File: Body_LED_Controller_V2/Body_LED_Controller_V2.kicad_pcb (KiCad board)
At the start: 4 copper layers, 123 x 78 mm, 101 parts, among them J1 Body Servos, J10 USB_B_Micro, J11 USB_B_Micro, J12 UnSW_BATT_IN, J13 Batt Level LEDS, J14 DomeControllerUSB, J15 DomePlateControllerUSB, J16 UnSW_BATT_PASS, J17 RADH_POW, J18 RASP_POW, J19 5V_OUT_3, J2 Body Servos, J20 ICSP, J21 DomeElectronicsPowerIn, J22 DB25_Female_MountingHoles, J23 Amplifier_POW, J24 Future, J25 Stealth, J26 RADH, J27 VU Data Panel, J3 Conn_02x10_Odd_Even, J4 LDP, J5 Coin Slots, J6 Batt Level LEDS, J7 Data Panel/ CBI, J8 Spectrum Analyzer, J9 Maintenance, SW1 SW_Push, SW2 SW_Push, U1 ATMEGA256016AU, U14 D36V50F5-STEPDOWN, U2 CH340C, U3 CJ2301_S1, U4 ESP32-WROOM-32D_16MB_, U5 CH340C, U6 UMH3N, U7 ME6211C33M5G, U8 CJ2301_S1, Y1 16MHz

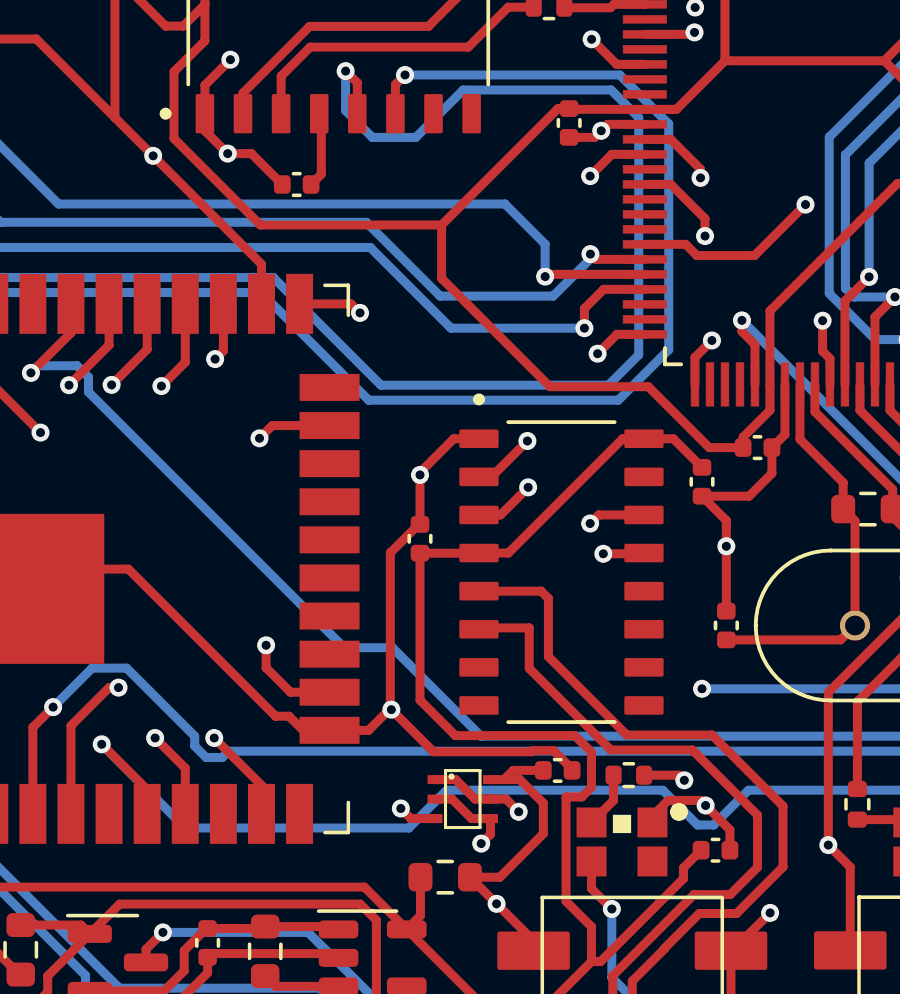
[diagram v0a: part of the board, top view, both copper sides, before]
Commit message: Added custom libraries and updated the Kill Switch (Remote)
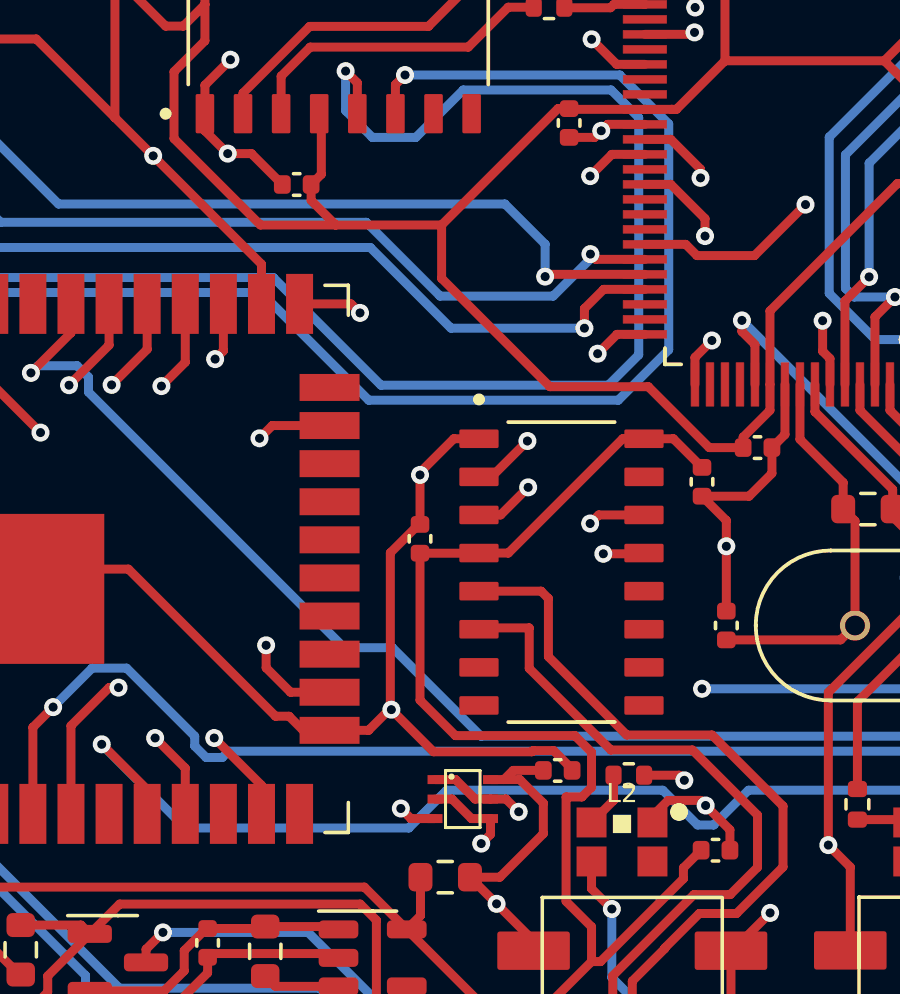
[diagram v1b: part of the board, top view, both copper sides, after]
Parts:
- J22: value DB25_Female_MountingHoles -> DB25_Male_MountingHoles
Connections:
- C5 pad 1: Net-(C5-Pad1) -> +5V_BL
- U2 pad 4: Net-(C5-Pad1) -> +5V_BL
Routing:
- net +5V_BL: track 154.4 -> 158.6 mm
- net Net-(C5-Pad1): track 2.53 -> 0.00 mm

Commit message: Working on boards
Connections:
- C5 pad 1: +5V_BL -> Net-(C5-Pad1)
- U2 pad 4: +5V_BL -> Net-(C5-Pad1)
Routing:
- net +5V_BL: track 158.6 -> 154.4 mm
- net Net-(C5-Pad1): track 0.00 -> 2.53 mm
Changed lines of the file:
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@@
   (net 190 "unconnected-(U1-Pad43)")
   (net 191 "unconnected-(U1-Pad44)")
+  (net 192 "Net-(C5-Pad1)")
   (footprint "Resistor_SMD:R_0402_1005Metric" (layer "F.Cu")
     (at 170.47 58.04 90)
@@
     (fp_line (start -0.5 0.25) (end -0.5 -0.25) (layer "F.Fab") (width 0.1))
     (pad "1" smd roundrect locked (at -0.48 0 180) (size 0.56 0.62) (layers "F.Cu" "F.Paste" "F.Mask") (roundrect_rratio 0.25)
-      (net 24 "+5V_BL") (pintype "passive"))
+      (net 192 "Net-(C5-Pad1)") (pintype "passive"))
     (pad "2" smd roundrect locked (at 0.48 0 180) (size 0.56 0.62) (layers "F.Cu" "F.Paste" "F.Mask") (roundrect_rratio 0.25)
       (net 2 "GND") (pintype "passive"))
@@
       (net 75 "Net-(R2-Pad1)") (pinfunction "RXD") (pintype "input"))
     (pad "4" smd roundrect (at -2.75 -0.635 90) (size 1.31 0.62) (layers "F.Cu" "F.Paste" "F.Mask") (roundrect_rratio 0.08)
-      (net 24 "+5V_BL") (pinfunction "V3") (pintype "power_in"))
+      (net 192 "Net-(C5-Pad1)") (pinfunction "V3") (pintype "power_in"))
     (pad "5" smd roundrect (at -2.75 0.635 90) (size 1.31 0.62) (layers "F.Cu" "F.Paste" "F.Mask") (roundrect_rratio 0.08)
       (net 48 "D+_BL") (pinfunction "UD+") (pintype "bidirectional"))
@@
   (segment (start 122.245 75.987735) (end 118.556113 79.676622) (width 0.3) (layer "F.Cu") (net 24))
   (segment (start 120.55 107.56) (end 122.75 107.56) (width 0.3) (layer "F.Cu") (net 24))
-  (segment (start 99.45 83.8) (end 99.79 83.46) (width 0.3) (layer "F.Cu") (net 24))
   (segment (start 122.245 75.125) (end 122.245 75.987735) (width 0.3) (layer "F.Cu") (net 24))
-  (segment (start 99.79 81.51) (end 99.72 81.44) (width 0.3) (layer "F.Cu") (net 24))
   (segment (start 122.674491 83.795) (end 118.556113 79.676622) (width 0.3) (layer "F.Cu") (net 24))
-  (segment (start 99.79 83.46) (end 99.79 81.51) (width 0.3) (layer "F.Cu") (net 24))
   (segment (start 112.245 75.125) (end 112.245 74.015) (width 0.3) (layer "F.Cu") (net 24))
-  (segment (start 99.45 84.33) (end 100.27 85.15) (width 0.3) (layer "F.Cu") (net 24))
   (segment (start 135.73 105.82) (end 135.17 105.26) (width 0.3) (layer "F.Cu") (net 24))
   (segment (start 141.9125 105.16) (end 141.27 105.16) (width 0.3) (layer "F.Cu") (net 24))
   (segment (start 95.19 78.52) (end 95.91 77.8) (width 0.3) (layer "F.Cu") (net 24))
   (segment (start 113.85 92.57) (end 112.72 92.57) (width 0.3) (layer "F.Cu") (net 24))
-  (segment (start 99.45 83.8) (end 99.45 84.33) (width 0.3) (layer "F.Cu") (net 24))
   (segment (start 94.88 80.04) (end 94.88 82.27) (width 0.3) (layer "F.Cu") (net 24))
   (segment (start 135.5102 101.2085) (end 135.5102 104.3002) (width 0.3) (layer "F.Cu") (net 24))
@@
   (segment (start 86.71 85.46) (end 88.698548 85.46) (width 0.3) (layer "In1.Cu") (net 184))
   (segment (start 85.33 95.91) (end 85.33 86.84) (width 0.3) (layer "In1.Cu") (net 184))
+  (segment (start 99.45 83.8) (end 99.79 83.46) (width 0.3) (layer "F.Cu") (net 192))
+  (segment (start 99.79 81.51) (end 99.72 81.44) (width 0.3) (layer "F.Cu") (net 192))
+  (segment (start 99.79 83.46) (end 99.79 81.51) (width 0.3) (layer "F.Cu") (net 192))
   (zone (net 1) (net_name "+12V") (layer "F.Cu") (hatch edge 0.508)
     (connect_pads (clearance 0.7))
